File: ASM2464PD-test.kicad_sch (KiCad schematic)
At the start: 52 parts, among them J1 USB_C_Receptacle, J2 Bus_M.2_Socket_M, U2 SPI_SOIC-8, U3 SPI_DFN-8

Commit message: Bunch more stuff copied from reference schematic
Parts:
- added C19: 220p, Capacitor_SMD:C_0201_0603Metric, symbol Device:C_Small
- added C20: 10p, Capacitor_SMD:C_0201_0603Metric, symbol Device:C_Small
- added C21: 1u, Capacitor_SMD:C_0201_0603Metric, symbol Device:C_Small
- added R22, R24, R25: 10k, Resistor_SMD:R_0201_0603Metric, symbol Device:R_Small
- added R23: 1k, Resistor_SMD:R_0201_0603Metric, symbol Device:R_Small
- added R26, R27, R28, R29, R30: 4.7k, Resistor_SMD:R_0201_0603Metric, symbol Device:R_Small
- added R31: 12.1k, Resistor_SMD:R_0201_0603Metric, symbol Device:R_Small
- added R32: 100k, Resistor_SMD:R_0201_0603Metric, symbol Device:R_Small
- added TP1: UART_RX, symbol Connector:TestPoint
- added TP2: GPIO1, symbol Connector:TestPoint
- added TP3: GPIO2, symbol Connector:TestPoint
- added TP4: I2C_DATA, symbol Connector:TestPoint
- added TP5: I2C_CLK, symbol Connector:TestPoint
- added Y1: 25MHz, Crystal:Crystal_SMD_3225-4Pin_3.2x2.5mm, symbol Device:Crystal_GND24
- D1, D2, D3, D4, D5, D6, D7, D8: now not fitted
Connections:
- net +3.3V: now also R22.1, R24.1, R25.1, R26.2, R27.2, R32.2
- net GND: now also C19.2, C21.2, R23.2, R28.2, R29.2, R30.2, R31.2, Y1.2, Y1.4
- net PERST#: now also C19.1, R22.2, R23.1
- net SPI_DO: now also R26.1, R29.1
- net GPIO22: now reaches R21.1
- net GPIO22: now also U1.A13 (GPIO22), R25.2
- net GPIO8: now reaches R20.1
- net GPIO8: now also U1.A19 (GPIO8), R24.2
- net UREXT: now reaches U1.AA3 (REXT)
- net UREXT: now also R31.1
- net XI: now reaches U1.AA4 (XI)
- net XI: now also C20.2, Y1.3
- net GPIO2: now reaches U1.B1 (GPIO2)
- net GPIO2: now also TP3.1
- net GPIO1: now reaches U1.C1 (GPIO1)
- net GPIO1: now also TP2.1
- net RST#: now reaches U1.H1 (RST#)
- net RST#: now also C21.1, R32.1
- net XO: now reaches U1.Y4 (XO)
- net XO: now also C20.1, Y1.1
- net UART_RX: now reaches U1.A21 (UART_RX)
- net UART_RX: now also TP1.1
- net UART_TX: now reaches U1.B21 (UART_TX)
- net UART_TX: now also R27.1, R28.1
- net I2C_CLK: now reaches U1.E1 (I2C_CLK_P)
- net I2C_CLK: now also TP5.1
- net I2C_DATA: now reaches U1.F1 (I2C_DATA_P)
- net I2C_DATA: now also TP4.1
- new net TEST_EN: R30.1
- no-connect marks 0 -> 2
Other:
- note added: "H/W Strapping"
- note removed: "todo idk weird"

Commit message: more schematic work
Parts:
- added D10: LED3, symbol Device:LED
- added D9: LED1, symbol Device:LED
- added R33, R34: 1k, Resistor_SMD:R_0201_0603Metric, symbol Device:R_Small
- added TP10: GPIO25, symbol Connector:TestPoint
- added TP11: GPIO26, symbol Connector:TestPoint
- added TP6: GPIO15, symbol Connector:TestPoint
- added TP7: GPIO16, symbol Connector:TestPoint
- added TP8: GPIO17, symbol Connector:TestPoint
- added TP9: GPIO18, symbol Connector:TestPoint
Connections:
- net +3.3V: now also D10.2 (A), D9.2 (A)
- net GPIO3: now reaches U1.A1 (GPIO3)
- net GPIO3: now also R34.1
- net GPIO25: now reaches U1.A16 (GPIO25)
- net GPIO25: now also TP10.1
- net GPIO26: now reaches U1.A17 (GPIO26)
- net GPIO26: now also TP11.1
- net GPIO15: now reaches U1.A6 (GPIO15)
- net GPIO15: now also TP6.1
- net GPIO16: now reaches U1.A7 (GPIO16)
- net GPIO16: now also TP7.1
- net GPIO17: now reaches U1.A8 (GPIO17)
- net GPIO17: now also TP8.1
- net GPIO18: now reaches U1.A9 (GPIO18)
- net GPIO18: now also TP9.1
- net GPIO0: now reaches U1.D1 (GPIO0)
- net GPIO0: now also R33.1
- new net: D9.1 (K), R33.2
- new net: D10.1 (K), R34.2
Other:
- note added: "Device LED"
- note added: "R/W LED"
- note added: "SPI ROM"
- moved on the sheet: C18, C20, C21, R17, R18, R26, R27, R28, R29, R30, R31, R32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

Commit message: more schematic work
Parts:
- removed C1, C2, C3, C4, C5, C6, C7, C8: 0.22u, Capacitor_SMD:C_0402_1005Metric, symbol Device:C_Small
- removed C10, C11, C12, C13, C14, C15, C16, C9: 0.33u, Capacitor_SMD:C_0201_0603Metric, symbol Device:C_Small
- removed C17, C21: 1u, Capacitor_SMD:C_0201_0603Metric, symbol Device:C_Small
- removed C18: 0.1u, Capacitor_SMD:C_0201_0603Metric, symbol Device:C_Small
- removed C19: 220p, Capacitor_SMD:C_0201_0603Metric, symbol Device:C_Small
- removed C20: 10p, Capacitor_SMD:C_0201_0603Metric, symbol Device:C_Small
- removed D1, D2, D3, D4, D5, D6, D7, D8: ~, Diode_SMD:D_0201_0603Metric, symbol Diode:ESD9B3.3ST5G
- removed D10: LED3, symbol Device:LED
- removed D9: LED1, symbol Device:LED
- removed J1: USB_C_Receptacle, Connector_USB:USB_C_Receptacle_Amphenol_12401610E4-2A, symbol Connector:USB_C_Receptacle
- removed J2: Bus_M.2_Socket_M, A_my_stuff:m-key, symbol Connector:Bus_M.2_Socket_M
- removed R1, R2, R3, R4, R5, R6, R7, R8: 220k, Resistor_SMD:R_0201_0603Metric, symbol Device:R_Small
- removed R10, R11, R12, R13, R14, R19, R20, R21, R9: 0Ω, Resistor_SMD:R_0201_0603Metric, symbol Device:R_Small
- removed R15, R17, R18, R26, R27, R28, R29, R30: 4.7k, Resistor_SMD:R_0201_0603Metric, symbol Device:R_Small
- removed R16, R22, R24, R25: 10k, Resistor_SMD:R_0201_0603Metric, symbol Device:R_Small
- removed R23, R33, R34: 1k, Resistor_SMD:R_0201_0603Metric, symbol Device:R_Small
- removed R31: 12.1k, Resistor_SMD:R_0201_0603Metric, symbol Device:R_Small
- removed R32: 100k, Resistor_SMD:R_0201_0603Metric, symbol Device:R_Small
- removed TP1: UART_RX, symbol Connector:TestPoint
- removed TP10: GPIO25, symbol Connector:TestPoint
- removed TP11: GPIO26, symbol Connector:TestPoint
- removed TP2: GPIO1, symbol Connector:TestPoint
- removed TP3: GPIO2, symbol Connector:TestPoint
- removed TP4: I2C_DATA, symbol Connector:TestPoint
- removed TP5: I2C_CLK, symbol Connector:TestPoint
- removed TP6: GPIO15, symbol Connector:TestPoint
- removed TP7: GPIO16, symbol Connector:TestPoint
- removed TP8: GPIO17, symbol Connector:TestPoint
- removed TP9: GPIO18, symbol Connector:TestPoint
- removed U1: ~, A_my_stuff:ASM2464PD, symbol A_my_stuff:ASM2464PD
- removed U2: SPI_SOIC-8, Package_SO:SOIC-8_5.23x5.23mm_P1.27mm, symbol A_my_stuff:SPI_flash
- removed U3: SPI_DFN-8, Package_DFN_QFN:DFN-8-1EP_3x2mm_P0.5mm_EP1.3x1.5mm, symbol A_my_stuff:SPI_flash
- removed Y1: 25MHz, Crystal:Crystal_SMD_3225-4Pin_3.2x2.5mm, symbol Device:Crystal_GND24
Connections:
- no-connect marks 2 -> 0
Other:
- added sheet Main (main.kicad_sch)
- added sheet Power (power.kicad_sch)
- note removed: "Device LED"
- note removed: "H/W Strapping"
- note removed: "R/W LED"
- note removed: "SPI ROM"

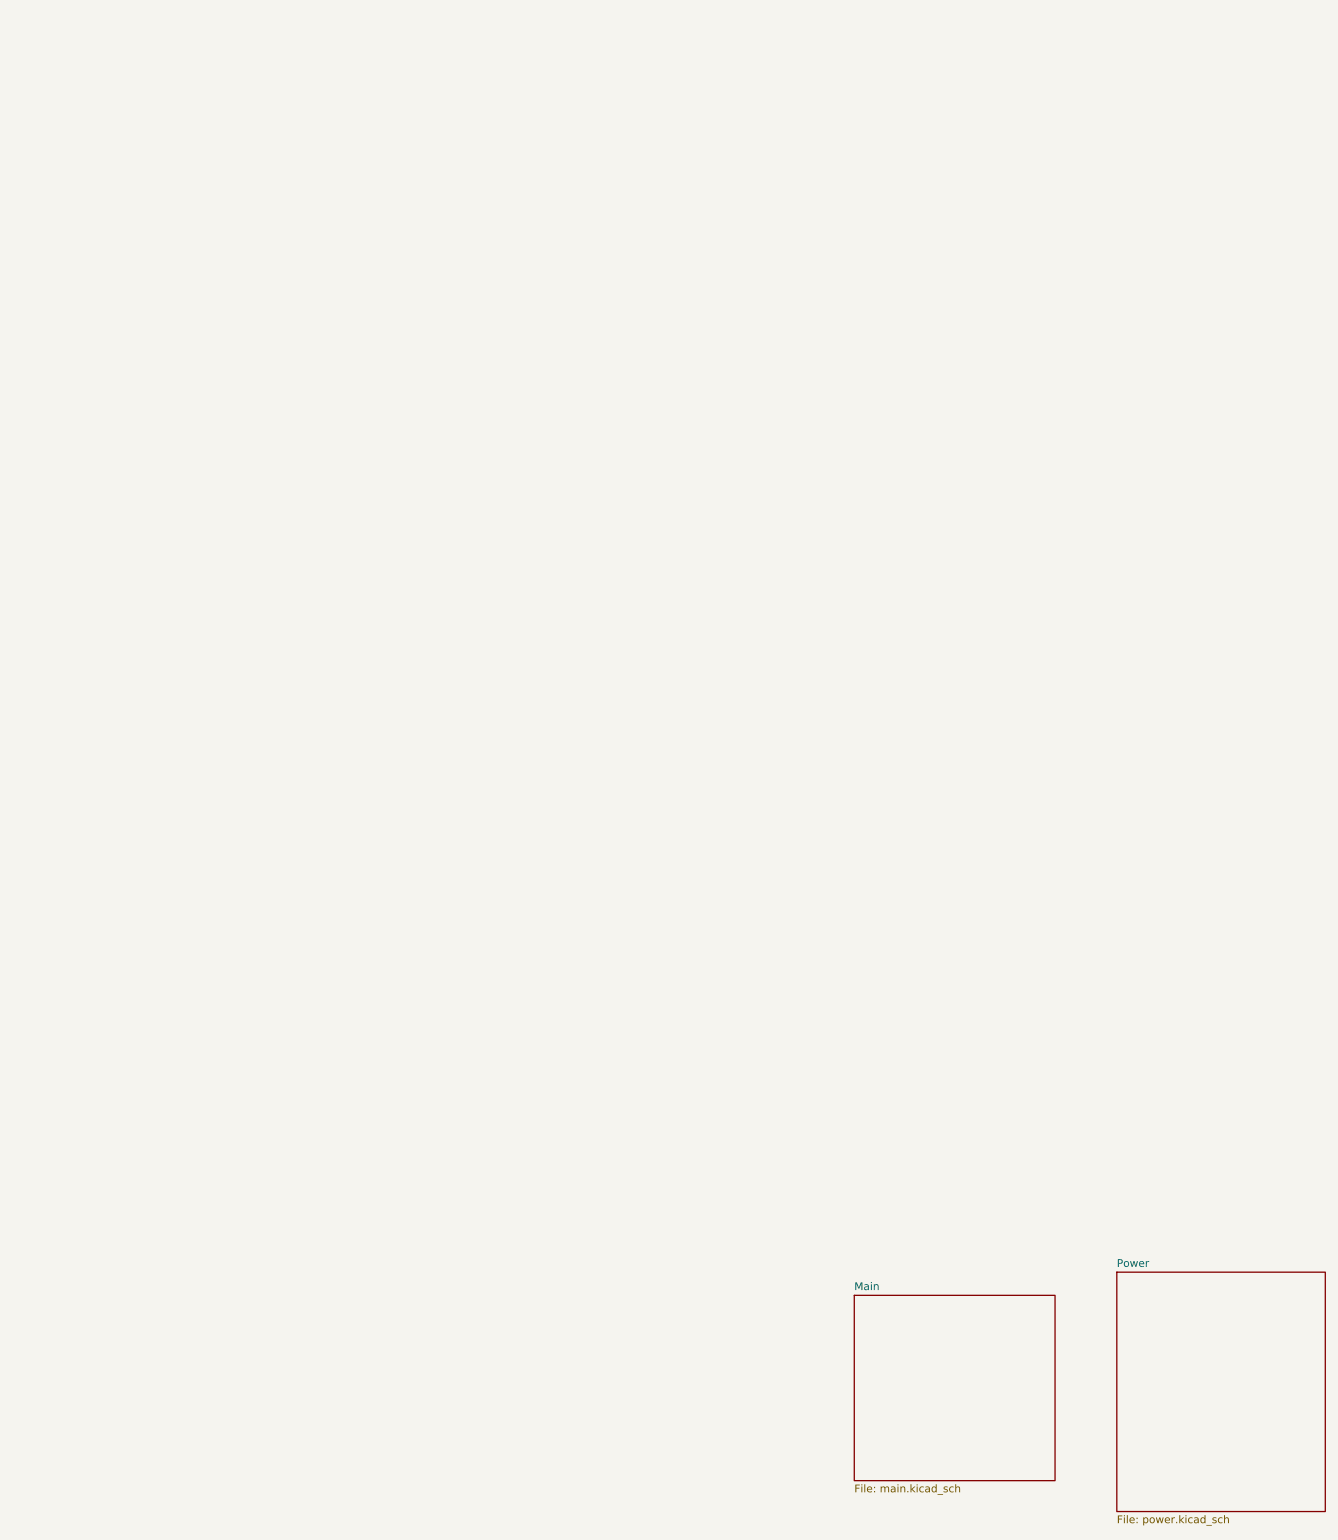
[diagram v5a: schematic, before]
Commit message: Cleaning up schematic a bit
Directly copying the reference schematic was stupid lol, what a mess
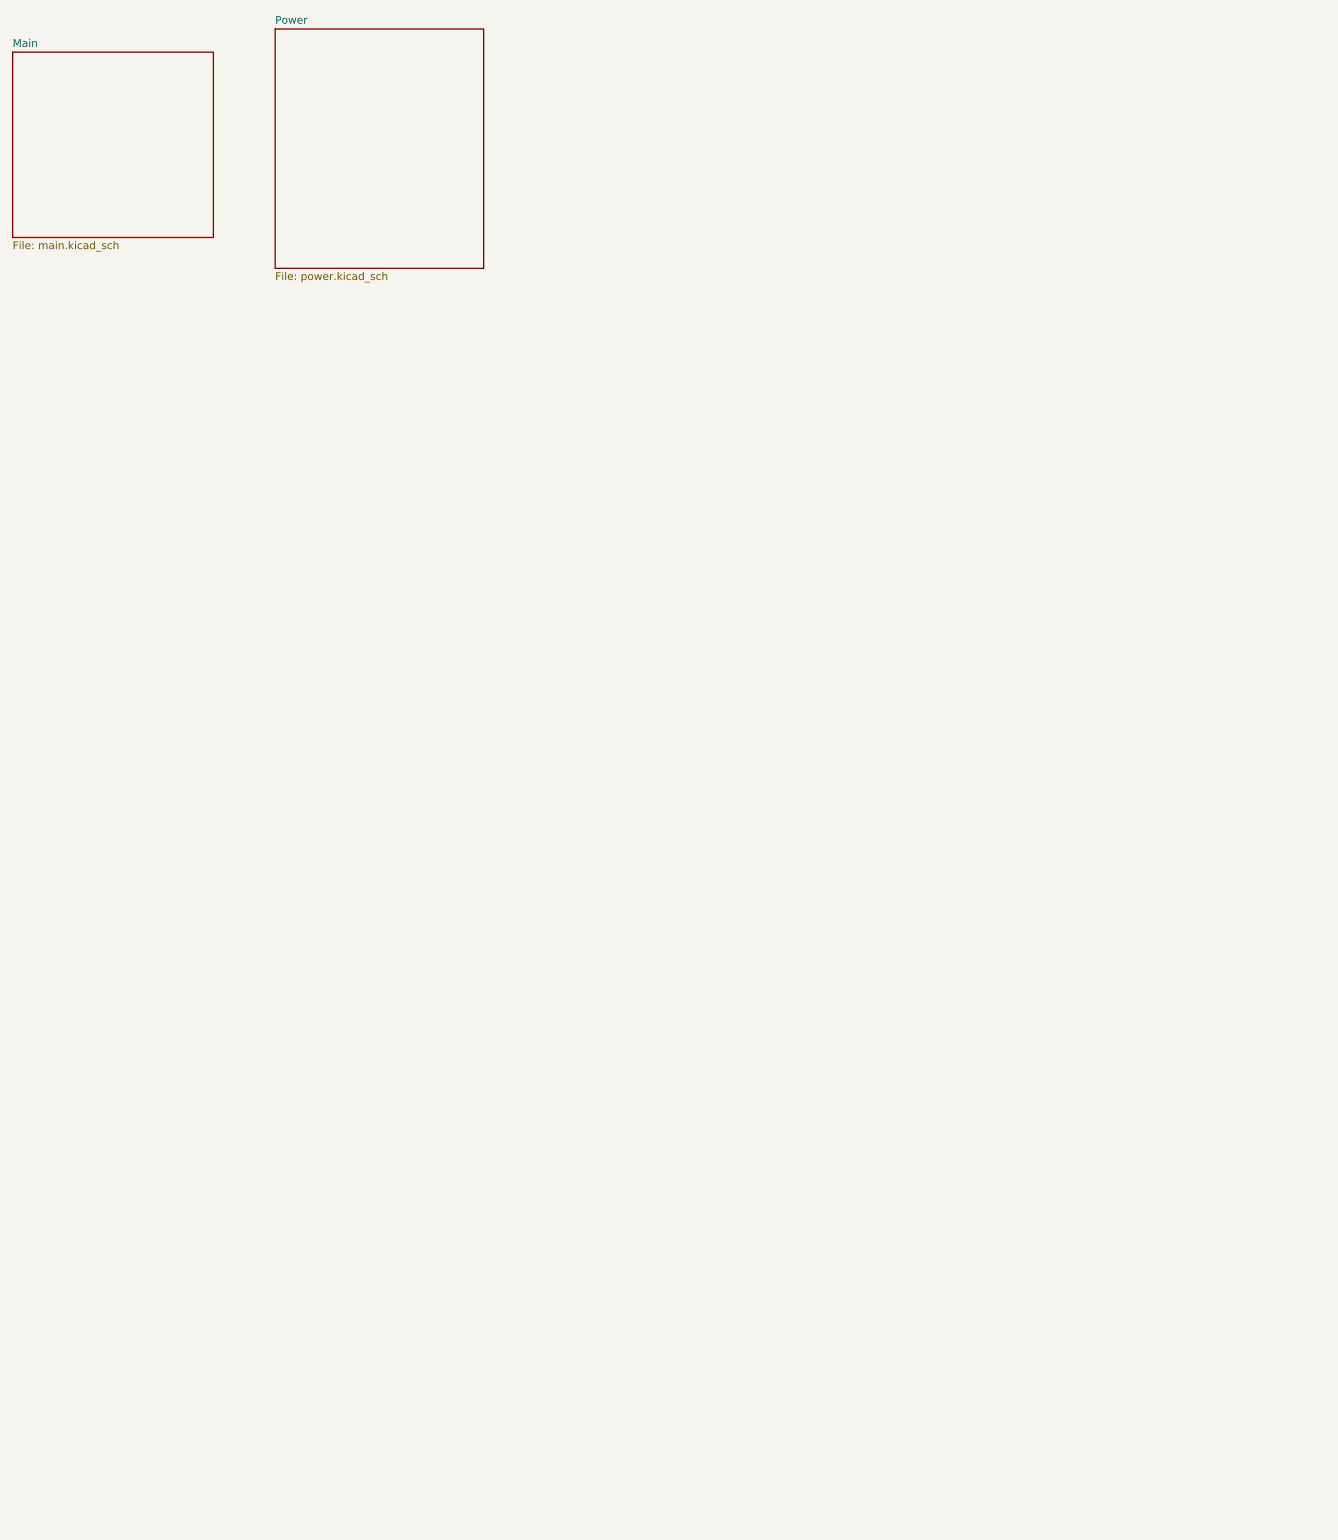
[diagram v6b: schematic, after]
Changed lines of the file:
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@@
 	(generator "eeschema")
 	(generator_version "9.0")
-	(paper "A2")
+	(paper "A4")
 	(title_block
 		(title "ASM2464PD-test")
@@
 	)
 	(sheet
-		(at 241.3 288.29)
+		(at 102.87 83.82)
 		(size 33.02 30.48)
 		(exclude_from_sim no)
@@
 		)
 		(property "Sheetname" "Main"
-			(at 241.3 287.5784 0)
+			(at 102.87 83.1084 0)
 			(effects
 				(font
@@
 		)
 		(property "Sheetfile" "main.kicad_sch"
-			(at 241.3 319.3546 0)
+			(at 102.87 114.8846 0)
 			(effects
 				(font
@@
 	)
 	(sheet
-		(at 284.48 284.48)
+		(at 146.05 80.01)
 		(size 34.29 39.37)
 		(exclude_from_sim no)
@@
 		)
 		(property "Sheetname" "Power"
-			(at 284.48 283.7684 0)
+			(at 146.05 79.2984 0)
 			(effects
 				(font
@@
 		)
 		(property "Sheetfile" "power.kicad_sch"
-			(at 284.48 324.4346 0)
+			(at 146.05 119.9646 0)
 			(effects
 				(font
